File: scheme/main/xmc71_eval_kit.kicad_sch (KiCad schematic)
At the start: 1 part

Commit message: added adc driver & output buffer with oe
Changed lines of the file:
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@@
+		)
+	)
+	(hierarchical_label "pwm_oe"
+		(shape output)
+		(at 264.16 92.71 0)
+		(effects
+			(font
+				(size 1.27 1.27)
+			)
+			(justify left)
 		)
 	)
@@
 	(hierarchical_label "do2"
 		(shape output)
-		(at 264.16 96.52 0)
+		(at 264.16 105.41 0)
 		(effects
 			(font
@@
 	(hierarchical_label "DCrelay"
 		(shape output)
-		(at 264.16 66.04 0)
+		(at 264.16 97.79 0)
+		(effects
+			(font
+				(size 1.27 1.27)
+			)
+			(justify left)
+		)
+	)
+	(hierarchical_label "oe"
+		(shape output)
+		(at 264.16 109.22 0)
 		(effects
 			(font
@@
 	(hierarchical_label "do1"
 		(shape output)
-		(at 264.16 92.71 0)
+		(at 264.16 101.6 0)
 		(effects
 			(font

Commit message: control boards symbols & footprints updated
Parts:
- BRD3: footprint (none) -> main:XMC71_EVAL_KIT_V1

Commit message: sheets titles
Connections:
- net Iu: now also BRD3.J2_2 (A1_ARD)
- net Iv: now also BRD3.J2_3 (A2_ARD)
- net Iw: now also BRD3.J2_4 (A3_ARD)
- net pwm_uh: now also BRD3.J21_38 (P3_5)
- net pwm_ul: now also BRD3.J21_40 (P4_0)
- net pwm_vh: now also BRD3.J23_35 (P17_6)
- net pwm_vl: now also BRD3.J23_2 (P17_7)
- net pwm_wh: now also BRD3.J21_34 (P3_3)
- net pwm_wl: now also BRD3.J21_36 (P3_4)
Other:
- title: (none) -> Плата KIT_XMC71_EVK_LITE_V1

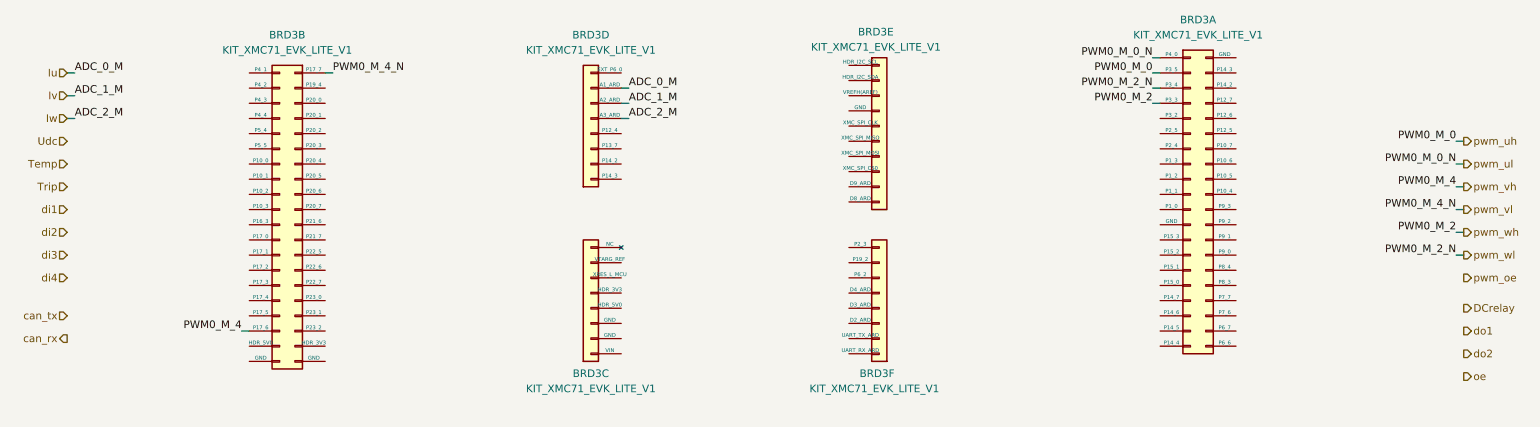
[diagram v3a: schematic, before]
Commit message: xmc71 evk lite v1 connections
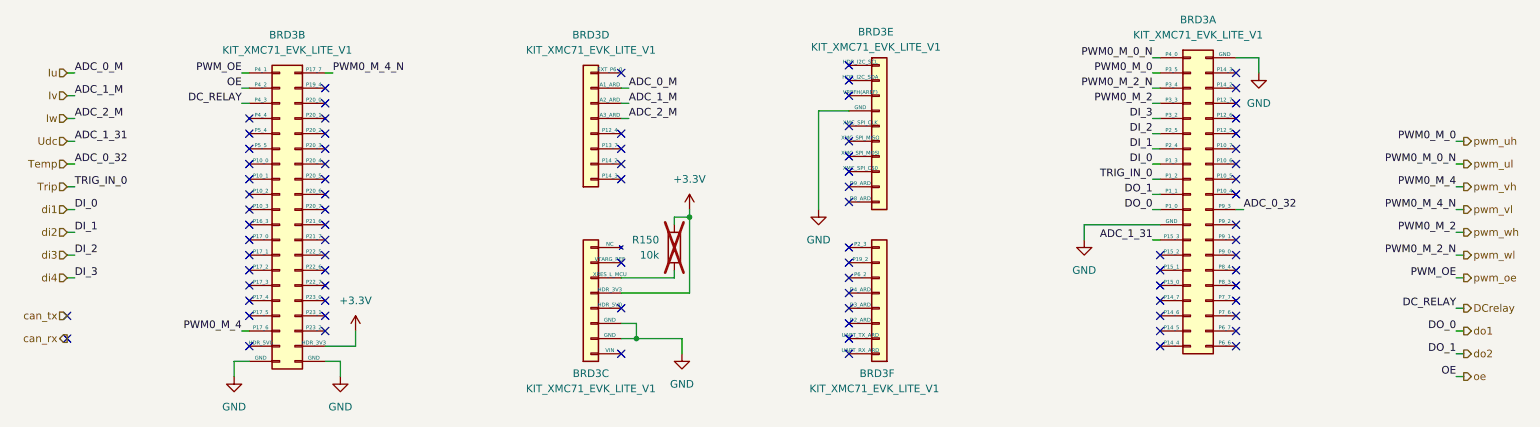
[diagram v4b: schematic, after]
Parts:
- added R150: 10k, Resistor_SMD:R_0805_2012Metric, symbol Device:R
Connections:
- net DCrelay: now also BRD3.J23_5 (P4_3)
- net Temp: now also BRD3.J21_19 (P9_3)
- net Trip: now also BRD3.J21_24 (P1_2)
- net Udc: now also BRD3.J21_16 (P15_3)
- net di1: now also BRD3.J21_26 (P1_3)
- net di2: now also BRD3.J21_28 (P2_4)
- net di3: now also BRD3.J21_30 (P2_5)
- net di4: now also BRD3.J21_32 (P3_2)
- net do1: now also BRD3.J21_20 (P1_0)
- net do2: now also BRD3.J21_22 (P1_1)
- net oe: now also BRD3.J23_3 (P4_2)
- net pwm_oe: now also BRD3.J23_1 (P4_1)
- net GND: now reaches BRD3.J3_7 (GND)
- net GND: now also BRD3.J1_2 (GND), BRD3.J1_3 (GND), BRD3.J21_18 (GND), BRD3.J21_39 (GND), BRD3.J23_39 (GND), BRD3.J23_40 (GND)
- net +3.3V: now reaches BRD3.J23_38 (HDR_3V3)
- net +3.3V: now also BRD3.J1_5 (HDR_3V3), R150.2
- net at BRD3.J1_6 (XRES_L_MCU): now also R150.1
- no-connect marks 0 -> 84

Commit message: added analog input 0 && sheets sort
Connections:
- net ain0: now reaches BRD3.J21_13 (P9_0)
- no-connect marks 84 -> 83
